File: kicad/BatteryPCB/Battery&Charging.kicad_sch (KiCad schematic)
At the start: 29 parts, among them J1 USB4105-GF-A, J2 Conn_01x02_Pin, J3 Conn_01x02_Pin, J4 Conn_01x02_Pin, SW7 SS-12D00-G 4 E, U5 TPS7A4901DGNT, U7 MT3608, U8 TP4056

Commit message: Battery PCB "DRC Clean"
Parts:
- added J5: 5V, Connector_PinSocket_2.54mm:PinSocket_1x02_P2.54mm_Vertical, symbol Connector:Conn_01x02_Pin
- J2: value Conn_01x02_Pin -> BoostV
- J3: value Conn_01x02_Pin -> BatteryV
- J4: value Conn_01x02_Pin -> 24V
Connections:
- net GND: now also J5.1 (Pin_1)
- net VBUS_USB: now also J5.2 (Pin_2)
- net 24V renamed +24V
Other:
- moved on the sheet: C6

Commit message: Add mounting holes and 3 pin JST header for interPCB connection
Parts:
- added H1, H2, H3, H4: MountingHole, MountingHole:MountingHole_3.5mm, symbol Mechanical:MountingHole
- added J6: B3B-XH-A, B3B_XH_A:JST_B3B-XH-A, symbol B3B_XH_A:B3B-XH-A
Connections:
- net +24V: now also J6.3
- net Battery_Voltage: now also J6.1
- net GND: now also J6.2

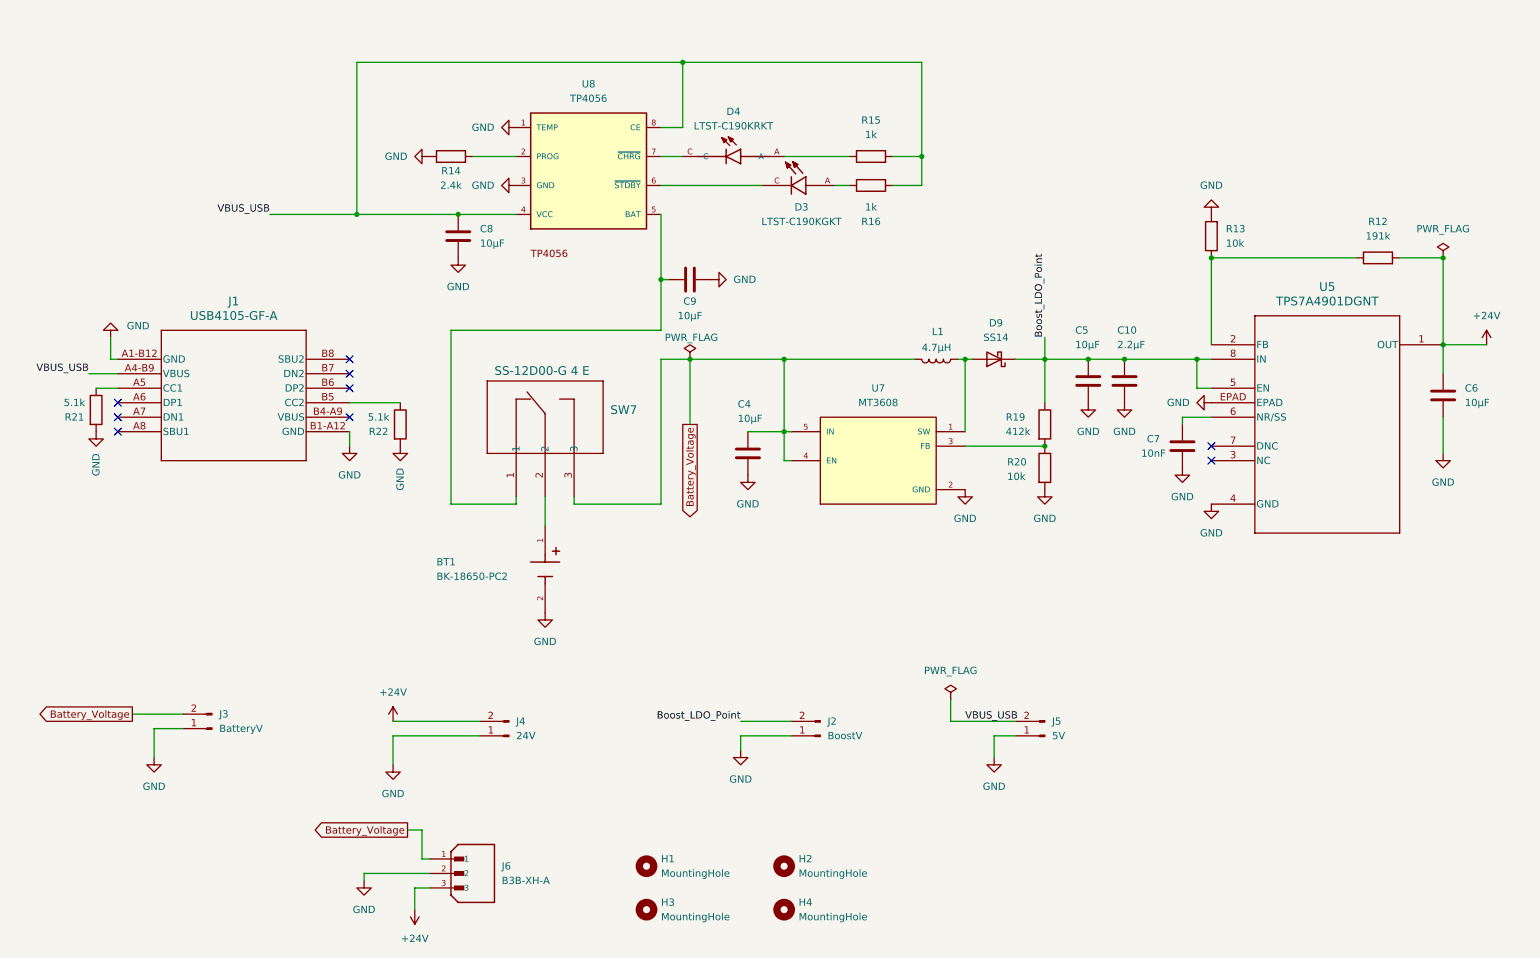
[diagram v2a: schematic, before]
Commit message: Changed switch and modified passive component values
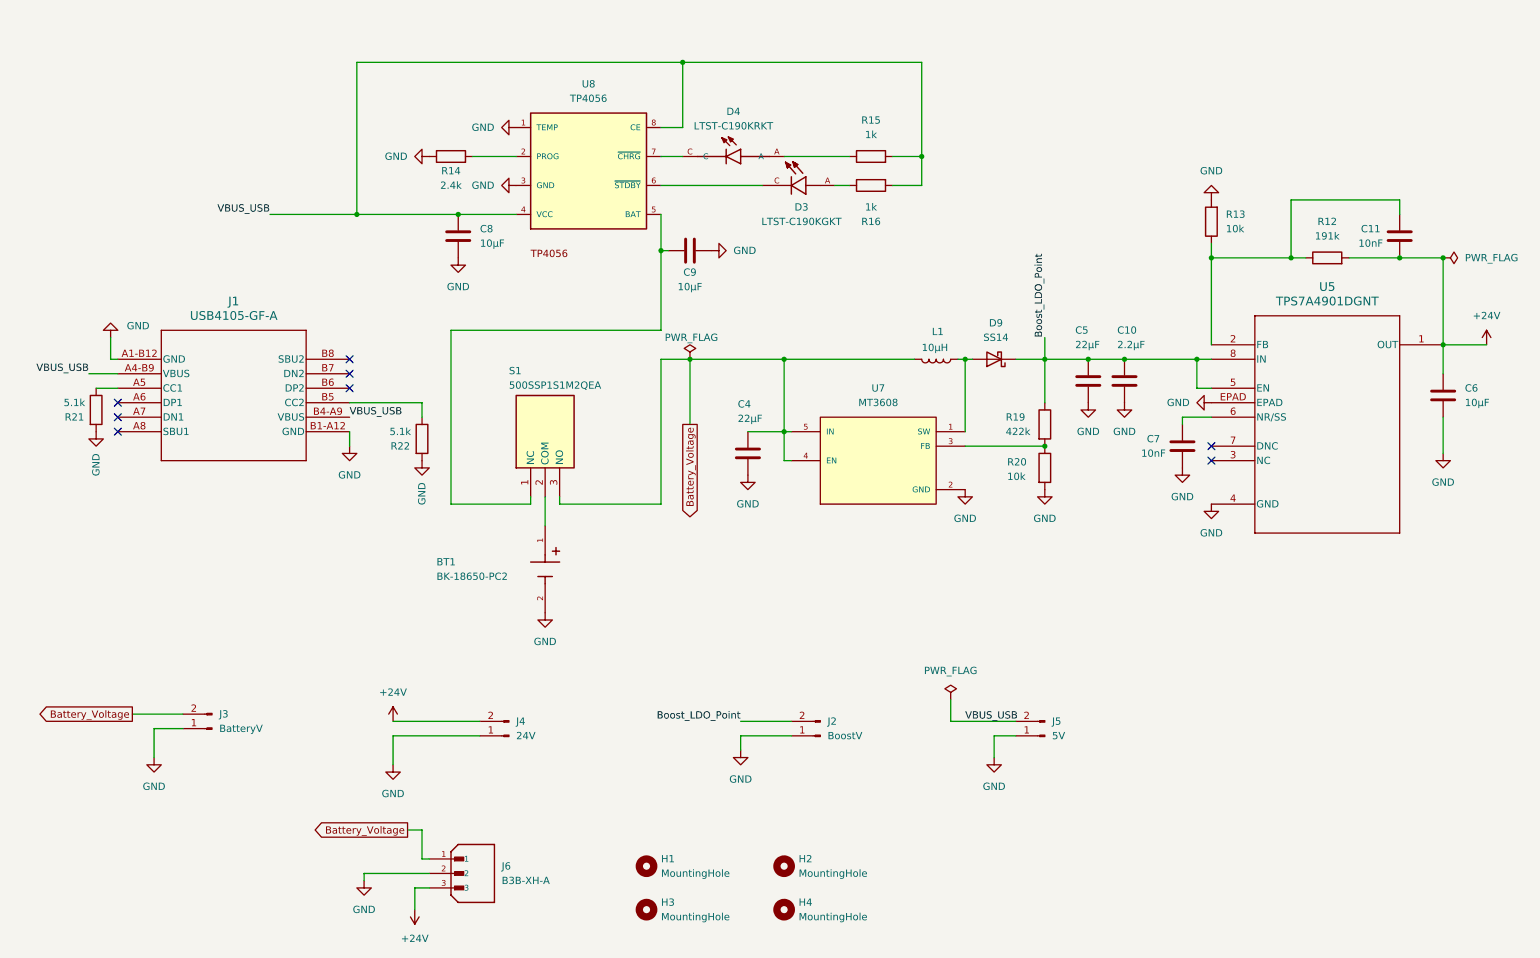
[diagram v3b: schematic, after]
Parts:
- removed SW7: SS-12D00-G 4 E, ul_SS-12D00-G-4-E:1P2T_SS-12D00_CNK, symbol ul_SS-12D00-G-4-E:SS-12D00-G_4_E
- added C11: 10nF, Capacitor_SMD:C_0805_2012Metric_Pad1.18x1.45mm_HandSolder, symbol Device:C
- added S1: 500SSP1S1M2QEA, 500SSP1S1M2QEA:500SSP1S1M2QEA, symbol 500SSP1S1M2QEA:500SSP1S1M2QEA
- C4, C5: value 10µF -> 22µF
- L1: value 4.7µH -> 10µH
- R19: value 412k -> 422k
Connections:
- net +24V: now also C11.2
- net Battery_Voltage: now also S1.3 (NO)
- net VBUS_USB: now also J1.B4-A9 (VBUS)
- net at R12.1, R13.1, U5.2 (FB): now also C11.1
- net at C9.1, U8.5 (BAT): now also S1.1 (NC)
- net at BT1.1: now also S1.2 (COM)
- no-connect marks 9 -> 8
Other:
- moved on the sheet: C9, R12, R13, R22

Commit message: Final PCB
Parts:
- removed H3, H4: MountingHole, MountingHole:MountingHole_3.5mm, symbol Mechanical:MountingHole
- removed L1: 10µH, SRN4018_4R7M:IND_BOURNS_SRN4018, symbol Device:L
- removed U8: TP4056, TP4056:SOT23-8, symbol TP4056:TP4056
- added L1: VLS6045EX-100M, VLS6045EX_100M:IND_VLS6045EX-100M, symbol VLS6045EX-100M:VLS6045EX-100M
- added U1: TP4056, TP4056:SOP127P600X175-9N, symbol TP4056:TP4056
- R16: value 1k -> 470
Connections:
- net Battery_Voltage: now also L1.1
- net GND: now also U1.1 (TEMP), U1.3 (GND), U1.9 (EP)
- net VBUS_USB: now also U1.4 (VCC), U1.8 (CE)
- net CHRG: now reaches D4.C
- net CHRG: now also U1.7 (~{CHRG})
- net at C9.1, S1.1 (NC): now also U1.5 (BAT)
- net at D9.2 (A), U7.1 (SW): now also L1.2
- net STDBY: now reaches D3.C
- net STDBY: now also U1.6 (~{STDBY})
- net at R14.2: now also U1.2 (PROG)
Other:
- moved on the sheet: D3, D4, R14, R15, R16
